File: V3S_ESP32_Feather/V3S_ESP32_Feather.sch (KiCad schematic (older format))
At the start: 12 parts, among them J2 Bat, J4 PWM, J6 UART, J8 I2C

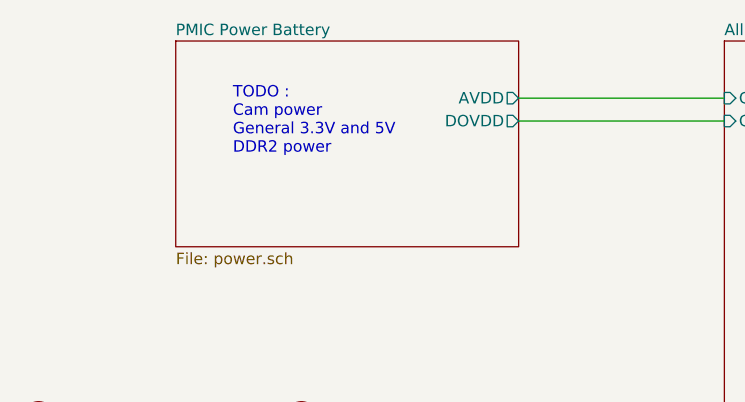
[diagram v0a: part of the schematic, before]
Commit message: Add i2c connector from V3s, fix sd card detection and remove todos
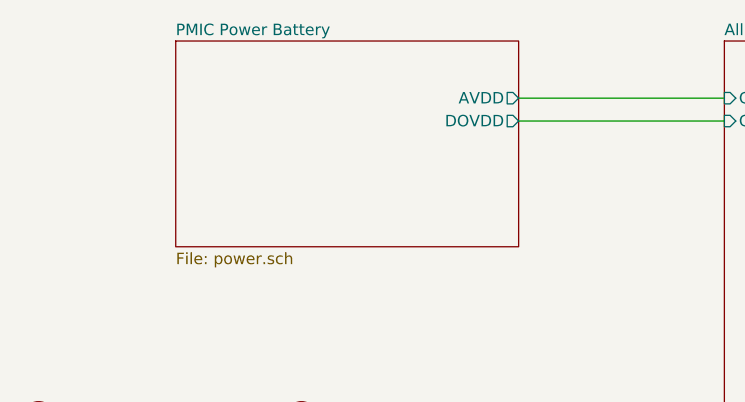
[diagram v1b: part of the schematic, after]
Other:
- note removed: "TODO :\nCam power\nGeneral 3.3V and 5V\nDDR2 power"
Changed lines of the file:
@@
 Text Label 3650 3750 2    50   ~ 0
 USB_D_P
-Text Notes 1500 1800 0    50   ~ 0
-TODO :\nCam power\nGeneral 3.3V and 5V\nDDR2 power
 $Comp
 L Connector:Conn_01x08_Female J4

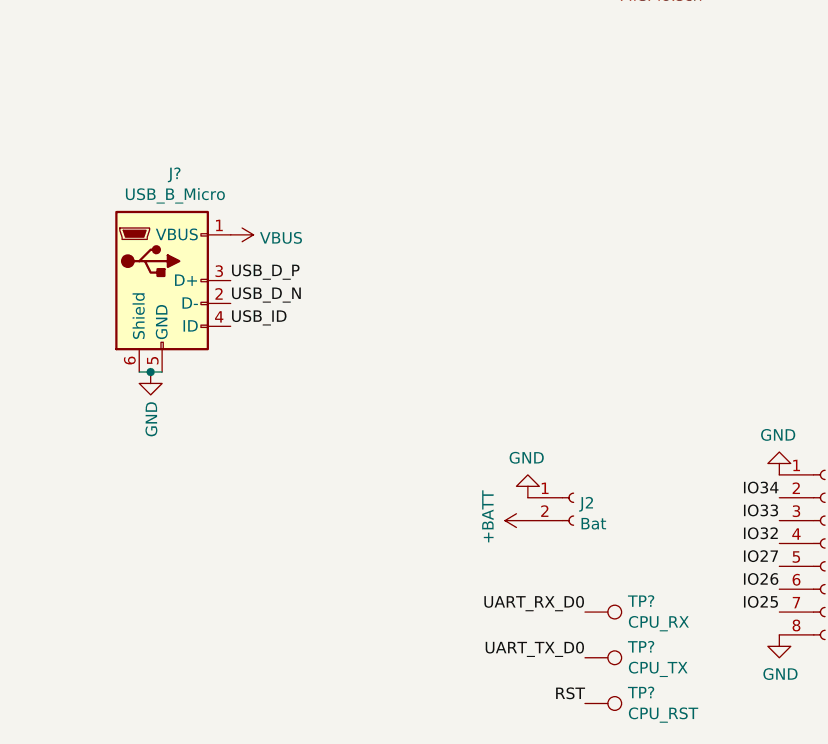
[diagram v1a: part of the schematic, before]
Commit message: Add more footprint, pcb format done, started component placement
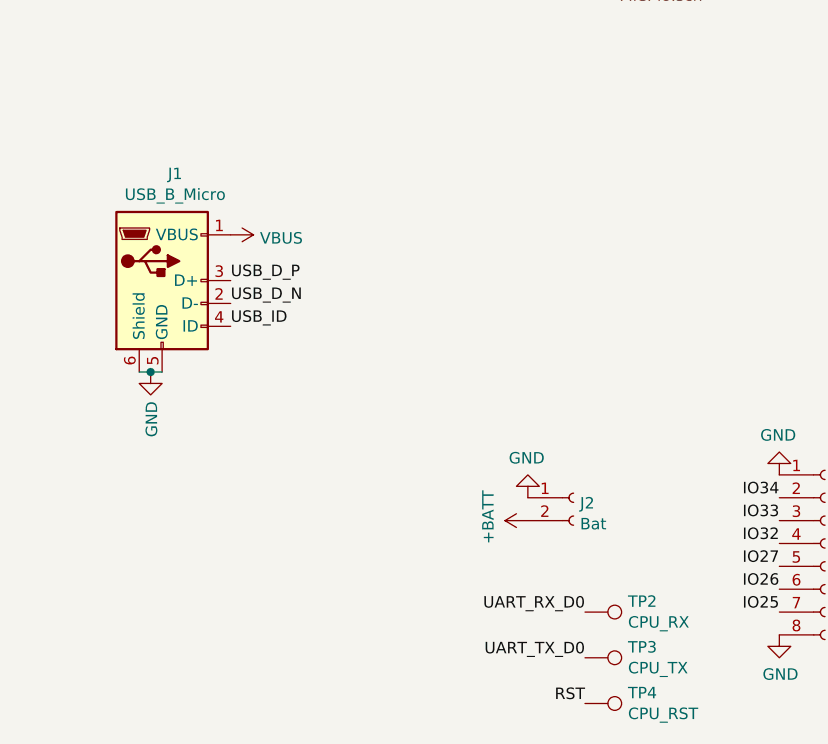
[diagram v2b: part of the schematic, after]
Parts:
- J1: renamed from J?; footprint (none) -> Connector_USB:USB_Micro-B_Molex-105017-0001
- J2: footprint Connector_PinHeader_2.54mm:PinHeader_1x02_P2.54mm_Vertical -> Connector_PinHeader_1.00mm:PinHeader_1x02_P1.00mm_Vertical
- J4: footprint Connector_PinHeader_2.54mm:PinHeader_1x08_P2.54mm_Vertical -> Connector_PinHeader_1.00mm:PinHeader_1x08_P1.00mm_Vertical
- J6: footprint Connector_PinSocket_2.54mm:PinSocket_1x04_P2.54mm_Vertical -> Connector_PinHeader_1.00mm:PinHeader_1x04_P1.00mm_Vertical
- J8: footprint Connector_PinSocket_2.54mm:PinSocket_1x04_P2.54mm_Vertical -> Connector_PinSocket_1.00mm:PinSocket_1x04_P1.00mm_Vertical
- TP2, TP3, TP4: renamed from TP?; footprint (none) -> TestPoint:TestPoint_Pad_D1.0mm
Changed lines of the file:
@@
 F 0 "J4" H 4578 6376 50  0000 L CNN
 F 1 "PWM" H 4578 6285 50  0000 L CNN
-F 2 "Connector_PinHeader_2.54mm:PinHeader_1x08_P2.54mm_Vertical" H 4550 6400 50  0001 C CNN
+F 2 "Connector_PinHeader_1.00mm:PinHeader_1x08_P1.00mm_Vertical" H 4550 6400 50  0001 C CNN
 F 3 "~" H 4550 6400 50  0001 C CNN
 	1    4550 6400
@@
 F 0 "J2" H 3478 6176 50  0000 L CNN
 F 1 "Bat" H 3478 6085 50  0000 L CNN
-F 2 "Connector_PinHeader_2.54mm:PinHeader_1x02_P2.54mm_Vertical" H 3450 6200 50  0001 C CNN
+F 2 "Connector_PinHeader_1.00mm:PinHeader_1x02_P1.00mm_Vertical" H 3450 6200 50  0001 C CNN
 F 3 "~" H 3450 6200 50  0001 C CNN
 	1    3450 6200
@@
 F 0 "J6" H 5678 6076 50  0000 L CNN
 F 1 "UART" H 5678 5985 50  0000 L CNN
-F 2 "Connector_PinSocket_2.54mm:PinSocket_1x04_P2.54mm_Vertical" H 5650 6100 50  0001 C CNN
+F 2 "Connector_PinHeader_1.00mm:PinHeader_1x04_P1.00mm_Vertical" H 5650 6100 50  0001 C CNN
 F 3 "~" H 5650 6100 50  0001 C CNN
 	1    5650 6100
@@
 F 0 "J8" H 5678 6726 50  0000 L CNN
 F 1 "I2C" H 5678 6635 50  0000 L CNN
-F 2 "Connector_PinSocket_2.54mm:PinSocket_1x04_P2.54mm_Vertical" H 5650 6750 50  0001 C CNN
+F 2 "Connector_PinSocket_1.00mm:PinSocket_1x04_P1.00mm_Vertical" H 5650 6750 50  0001 C CNN
 F 3 "~" H 5650 6750 50  0001 C CNN
 	1    5650 6750
@@
 $EndComp
 $Comp
-L Connector:TestPoint TP?
+L Connector:TestPoint TP2
 U 1 1 5D883927
 P 3500 6700
-F 0 "TP?" V 3454 6888 50  0000 L CNN
+F 0 "TP2" V 3454 6888 50  0000 L CNN
 F 1 "CPU_RX" V 3545 6888 50  0000 L CNN
-F 2 "" H 3700 6700 50  0001 C CNN
+F 2 "TestPoint:TestPoint_Pad_D1.0mm" H 3700 6700 50  0001 C CNN
 F 3 "~" H 3700 6700 50  0001 C CNN
 	1    3500 6700
@@
 $EndComp
 $Comp
-L Connector:TestPoint TP?
+L Connector:TestPoint TP3
 U 1 1 5D8846E9
 P 3500 6900
-F 0 "TP?" V 3454 7088 50  0000 L CNN
+F 0 "TP3" V 3454 7088 50  0000 L CNN
 F 1 "CPU_TX" V 3545 7088 50  0000 L CNN
-F 2 "" H 3700 6900 50  0001 C CNN
+F 2 "TestPoint:TestPoint_Pad_D1.0mm" H 3700 6900 50  0001 C CNN
 F 3 "~" H 3700 6900 50  0001 C CNN
 	1    3500 6900
@@
 $EndComp
 $Comp
-L Connector:TestPoint TP?
+L Connector:TestPoint TP4
 U 1 1 5D884C58
 P 3500 7100
-F 0 "TP?" V 3454 7288 50  0000 L CNN
+F 0 "TP4" V 3454 7288 50  0000 L CNN
 F 1 "CPU_RST" V 3545 7288 50  0000 L CNN
-F 2 "" H 3700 7100 50  0001 C CNN
+F 2 "TestPoint:TestPoint_Pad_D1.0mm" H 3700 7100 50  0001 C CNN
 F 3 "~" H 3700 7100 50  0001 C CNN
 	1    3500 7100
@@
 $EndComp
 $Comp
-L Connector:USB_B_Micro J?
+L Connector:USB_B_Micro J1
 U 1 1 5D8C9C3C
 P 1650 5250
-F 0 "J?" H 1707 5717 50  0000 C CNN
+F 0 "J1" H 1707 5717 50  0000 C CNN
 F 1 "USB_B_Micro" H 1707 5626 50  0000 C CNN
-F 2 "" H 1800 5200 50  0001 C CNN
+F 2 "Connector_USB:USB_Micro-B_Molex-105017-0001" H 1800 5200 50  0001 C CNN
 F 3 "~" H 1800 5200 50  0001 C CNN
 	1    1650 5250

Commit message: New component placement, progress on rooting
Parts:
- J2: footprint Connector_PinHeader_1.00mm:PinHeader_1x02_P1.00mm_Vertical -> Connector_JST:JST_SH_SM02B-SRSS-TB_1x02-1MP_P1.00mm_Horizontal
- J4: footprint Connector_PinHeader_1.00mm:PinHeader_1x08_P1.00mm_Vertical -> Connector_JST:JST_SH_SM08B-SRSS-TB_1x08-1MP_P1.00mm_Horizontal
- J6: footprint Connector_PinHeader_1.00mm:PinHeader_1x04_P1.00mm_Vertical -> Connector_JST:JST_SH_SM04B-SRSS-TB_1x04-1MP_P1.00mm_Horizontal
- J8: footprint Connector_PinSocket_1.00mm:PinSocket_1x04_P1.00mm_Vertical -> Connector_JST:JST_SH_SM04B-SRSS-TB_1x04-1MP_P1.00mm_Horizontal
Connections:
- net GND: no longer J4.1 (Pin_1)
- net IO25: now also J4.5 (Pin_5); no longer J4.7 (Pin_7)
- net IO27: now also J4.7 (Pin_7); no longer J4.5 (Pin_5)
- net IO32: now also J4.3 (Pin_3); no longer J4.4 (Pin_4)
- net IO33: now also J4.4 (Pin_4); no longer J4.3 (Pin_3)
- net IO34: now also J4.1 (Pin_1); no longer J4.2 (Pin_2)
- new net IO35: J4.2 (Pin_2)
- no-connect marks 0 -> 1

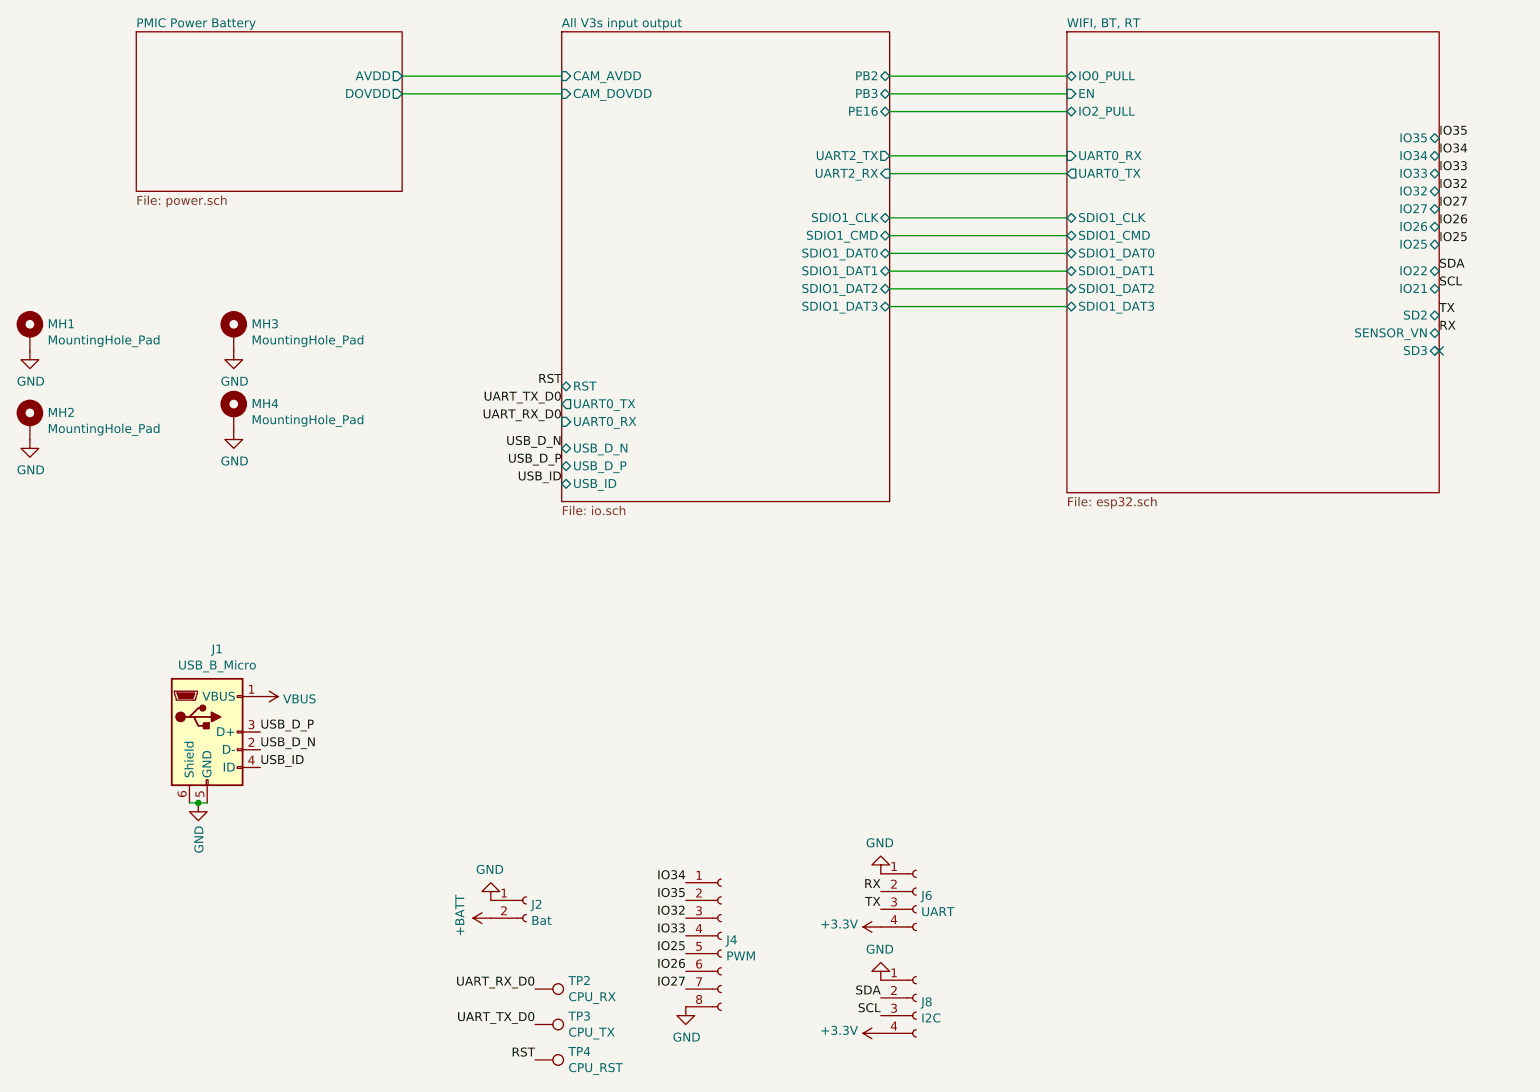
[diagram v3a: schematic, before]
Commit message: Change Max13030 and moove ESP32
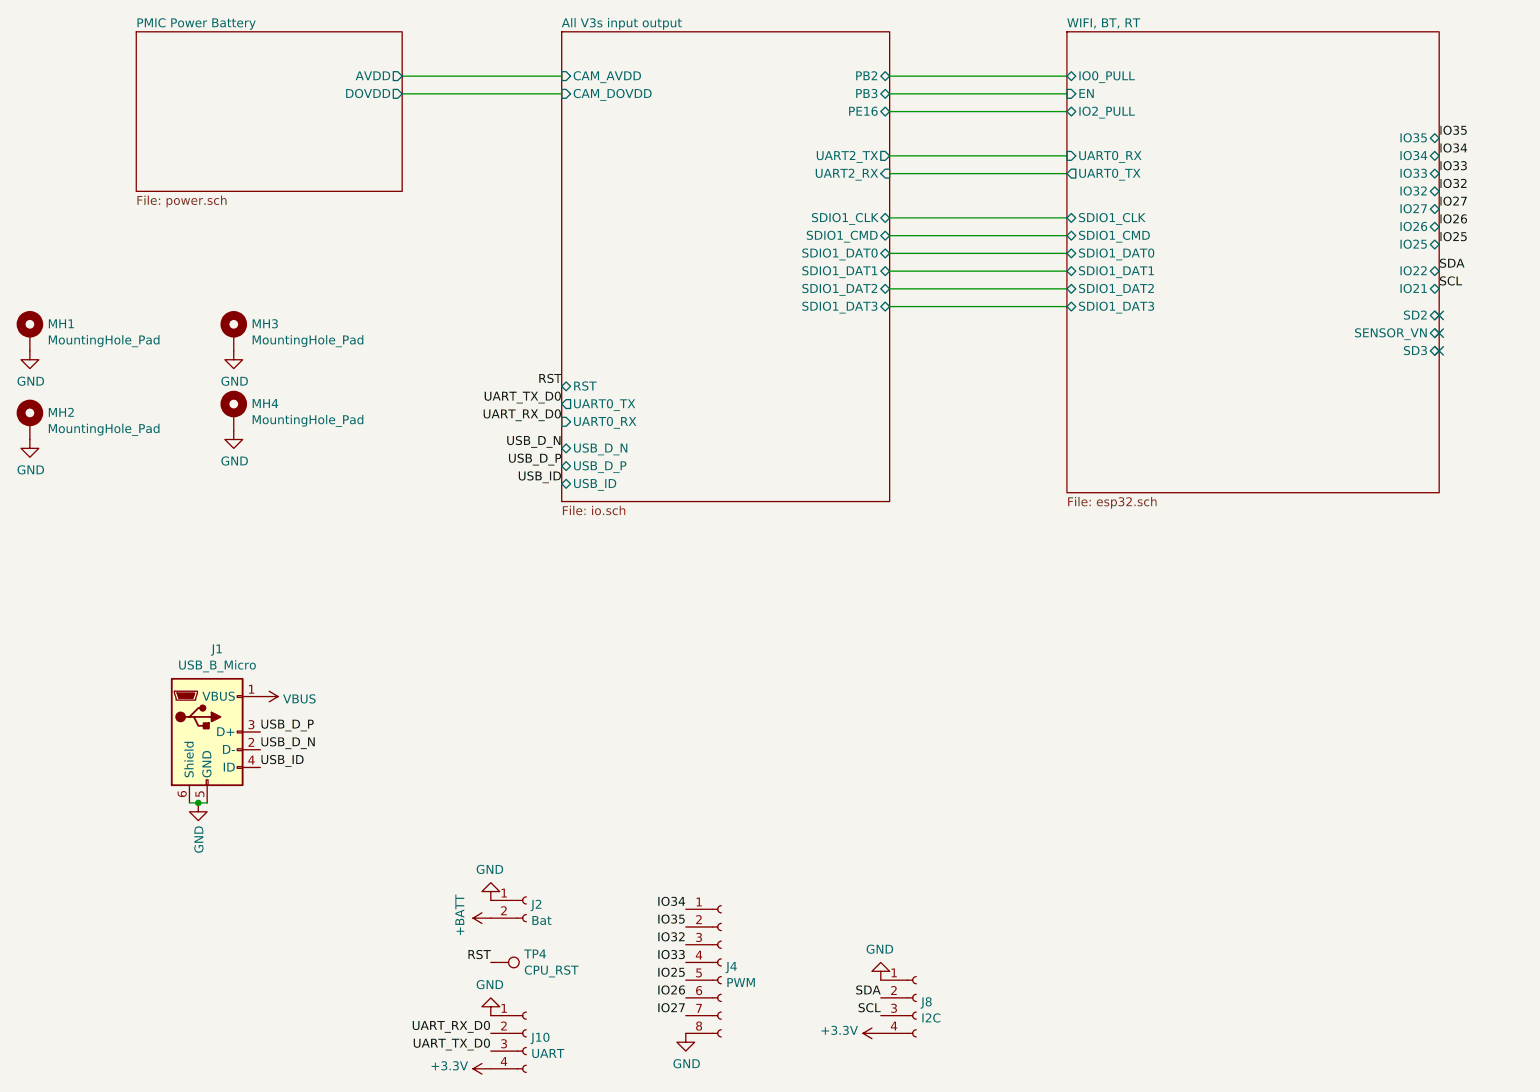
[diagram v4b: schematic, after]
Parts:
- removed J6: UART, Connector_JST:JST_SH_SM04B-SRSS-TB_1x04-1MP_P1.00mm_Horizontal, symbol Connector:Conn_01x04_Female
- removed TP2: CPU_RX, TestPoint:TestPoint_Pad_D1.0mm, symbol Connector:TestPoint
- removed TP3: CPU_TX, TestPoint:TestPoint_Pad_D1.0mm, symbol Connector:TestPoint
- added J10: UART, Connector_JST:JST_SH_SM04B-SRSS-TB_1x04-1MP_P1.00mm_Horizontal, symbol Connector:Conn_01x04_Female
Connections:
- net +3V3: now also J10.4 (Pin_4)
- net GND: now also J10.1 (Pin_1)
- net UART_RX_D0: now also J10.2 (Pin_2)
- net UART_TX_D0: now also J10.3 (Pin_3)
- no-connect marks 1 -> 3
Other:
- moved on the sheet: J4, TP4
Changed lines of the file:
@@
 Wire Wire Line
 	3650 1650 2750 1650
-Text Label 3500 7100 2    50   ~ 0
+Text Label 3250 6550 2    50   ~ 0
 RST
 Text Label 3650 3400 2    50   ~ 0
@@
 L Connector:Conn_01x08_Female J4
 U 1 1 5D7F05A5
-P 4550 6400
-F 0 "J4" H 4578 6376 50  0000 L CNN
-F 1 "PWM" H 4578 6285 50  0000 L CNN
-F 2 "Connector_JST:JST_SH_SM08B-SRSS-TB_1x08-1MP_P1.00mm_Horizontal" H 4550 6400 50  0001 C CNN
-F 3 "~" H 4550 6400 50  0001 C CNN
-	1    4550 6400
+P 4550 6550
+F 0 "J4" H 4578 6526 50  0000 L CNN
+F 1 "PWM" H 4578 6435 50  0000 L CNN
+F 2 "Connector_JST:JST_SH_SM08B-SRSS-TB_1x08-1MP_P1.00mm_Horizontal" H 4550 6550 50  0001 C CNN
+F 3 "~" H 4550 6550 50  0001 C CNN
+	1    4550 6550
 	1    0    0    -1
 $EndComp
@@
 Text Label 8600 2500 0    50   ~ 0
 IO25
-Text Label 4350 6400 2    50   ~ 0
+Text Label 4350 6550 2    50   ~ 0
 IO33
-Text Label 4350 6300 2    50   ~ 0
+Text Label 4350 6450 2    50   ~ 0
 IO32
-Text Label 4350 6700 2    50   ~ 0
+Text Label 4350 6850 2    50   ~ 0
 IO27
-Text Label 4350 6600 2    50   ~ 0
+Text Label 4350 6750 2    50   ~ 0
 IO26
-Text Label 4350 6500 2    50   ~ 0
+Text Label 4350 6650 2    50   ~ 0
 IO25
 $Comp
 L power:GND #PWR0125
 U 1 1 5D81A9F6
-P 4350 6800
-F 0 "#PWR0125" H 4350 6550 50  0001 C CNN
-F 1 "GND" H 4355 6627 50  0000 C CNN
-F 2 "" H 4350 6800 50  0001 C CNN
-F 3 "" H 4350 6800 50  0001 C CNN
-	1    4350 6800
+P 4350 6950
+F 0 "#PWR0125" H 4350 6700 50  0001 C CNN
+F 1 "GND" H 4355 6777 50  0000 C CNN
+F 2 "" H 4350 6950 50  0001 C CNN
+F 3 "" H 4350 6950 50  0001 C CNN
+	1    4350 6950
 	1    0    0    -1
 $EndComp
 Text Label 8600 2000 0    50   ~ 0
 IO34
-Text Label 4350 6100 2    50   ~ 0
+Text Label 4350 6250 2    50   ~ 0
 IO34
 Text Label 8600 2650 0    50   ~ 0
@@
 L Connector:TestPoint TP4
 U 1 1 5D884C58
-P 3500 7100
-F 0 "TP4" V 3454 7288 50  0000 L CNN
-F 1 "CPU_RST" V 3545 7288 50  0000 L CNN
-F 2 "TestPoint:TestPoint_Pad_D1.0mm" H 3700 7100 50  0001 C CNN
-F 3 "~" H 3700 7100 50  0001 C CNN
-	1    3500 7100
+P 3250 6550
+F 0 "TP4" V 3204 6738 50  0000 L CNN
+F 1 "CPU_RST" V 3295 6738 50  0000 L CNN
+F 2 "TestPoint:TestPoint_Pad_D1.0mm" H 3450 6550 50  0001 C CNN
+F 3 "~" H 3450 6550 50  0001 C CNN
+	1    3250 6550
 	0    1    1    0
 $EndComp
@@
 $EndSheet
 NoConn ~ 8600 3100
-Text Label 4350 6200 2    50   ~ 0
+Text Label 4350 6350 2    50   ~ 0
 IO35
 Text Label 8600 1900 0    50   ~ 0
 IO35
-$Comp
-L Connector:Conn_01x04_Female J6
-U 1 1 5D902445
-P 5650 6150
-F 0 "J6" H 5678 6126 50  0000 L CNN
-F 1 "UART" H 5678 6035 50  0000 L CNN
-F 2 "Connector_JST:JST_SH_SM04B-SRSS-TB_1x04-1MP_P1.00mm_Horizontal" H 5650 6150 50  0001 C CNN
-F 3 "~" H 5650 6150 50  0001 C CNN
-	1    5650 6150
-	1    0    0    -1
-$EndComp
-$Comp
-L power:GND #PWR0119
-U 1 1 5D90244D
-P 5450 6050
-F 0 "#PWR0119" H 5450 5800 50  0001 C CNN
-F 1 "GND" H 5455 5877 50  0000 C CNN
-F 2 "" H 5450 6050 50  0001 C CNN
-F 3 "" H 5450 6050 50  0001 C CNN
-	1    5450 6050
+Text Label 3250 6950 2    50   ~ 0
+UART_RX_D0
+Text Label 3250 7050 2    50   ~ 0
+UART_TX_D0
+$Comp
+L Connector:Conn_01x04_Female J10
+U 1 1 5D8B77E7
+P 3450 6950
+F 0 "J10" H 3478 6926 50  0000 L CNN
+F 1 "UART" H 3478 6835 50  0000 L CNN
+F 2 "Connector_JST:JST_SH_SM04B-SRSS-TB_1x04-1MP_P1.00mm_Horizontal" H 3450 6950 50  0001 C CNN
+F 3 "~" H 3450 6950 50  0001 C CNN
+	1    3450 6950
+	1    0    0    -1
+$EndComp
+$Comp
+L power:GND #PWR0124
+U 1 1 5D8B77ED
+P 3250 6850
+F 0 "#PWR0124" H 3250 6600 50  0001 C CNN
+F 1 "GND" H 3255 6677 50  0000 C CNN
+F 2 "" H 3250 6850 50  0001 C CNN
+F 3 "" H 3250 6850 50  0001 C CNN
+	1    3250 6850
 	-1   0    0    1
 $EndComp
 $Comp
-L power:+3.3V #PWR0121
-U 1 1 5D902453
-P 5450 6350
-F 0 "#PWR0121" H 5450 6200 50  0001 C CNN
-F 1 "+3.3V" V 5465 6478 50  0000 L CNN
-F 2 "" H 5450 6350 50  0001 C CNN
-F 3 "" H 5450 6350 50  0001 C CNN
-	1    5450 6350
+L power:+3.3V #PWR0126
+U 1 1 5D8B77F3
+P 3250 7150
+F 0 "#PWR0126" H 3250 7000 50  0001 C CNN
+F 1 "+3.3V" V 3265 7278 50  0000 L CNN
+F 2 "" H 3250 7150 50  0001 C CNN
+F 3 "" H 3250 7150 50  0001 C CNN
+	1    3250 7150
 	0    -1   -1   0
 $EndComp
-Text Label 8600 2900 0    50   ~ 0
-TX
-Text Label 8600 3000 0    50   ~ 0
-RX
-Text Label 5450 6250 2    50   ~ 0
-TX
-Text Label 5450 6150 2    50   ~ 0
-RX
-$Comp
-L Connector:TestPoint TP3
-U 1 1 5D8846E9
-P 3500 6900
-F 0 "TP3" V 3454 7088 50  0000 L CNN
-F 1 "CPU_TX" V 3545 7088 50  0000 L CNN
-F 2 "TestPoint:TestPoint_Pad_D1.0mm" H 3700 6900 50  0001 C CNN
-F 3 "~" H 3700 6900 50  0001 C CNN
-	1    3500 6900
-	0    1    1    0
-$EndComp
-$Comp
-L Connector:TestPoint TP2
-U 1 1 5D883927
-P 3500 6700
-F 0 "TP2" V 3454 6888 50  0000 L CNN
-F 1 "CPU_RX" V 3545 6888 50  0000 L CNN
-F 2 "TestPoint:TestPoint_Pad_D1.0mm" H 3700 6700 50  0001 C CNN
-F 3 "~" H 3700 6700 50  0001 C CNN
-	1    3500 6700
-	0    1    1    0
-$EndComp
-Text Label 3500 6700 2    50   ~ 0
-UART_RX_D0
-Text Label 3500 6900 2    50   ~ 0
-UART_TX_D0
+NoConn ~ 8600 2900
+NoConn ~ 8600 3000
 $EndSCHEMATC
